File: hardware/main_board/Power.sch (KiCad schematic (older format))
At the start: 12 parts, among them U201 LM1117-5.0

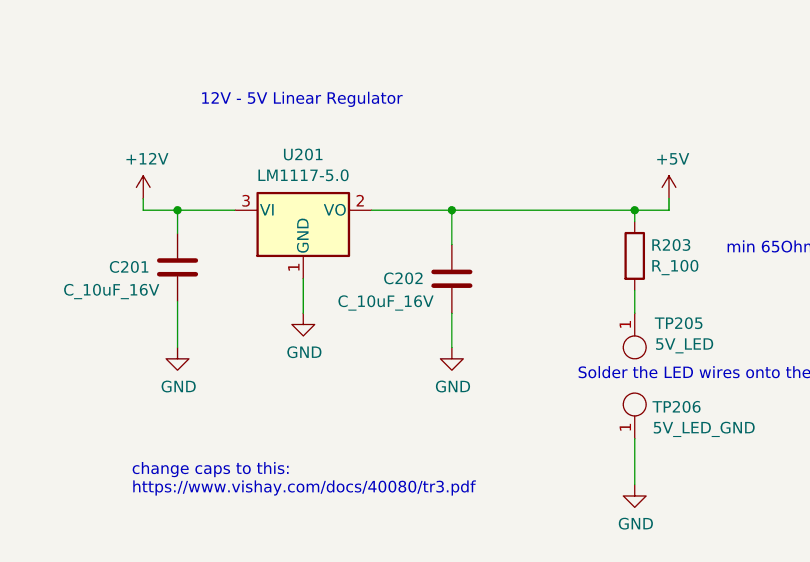
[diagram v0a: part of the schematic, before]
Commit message: added connector for powering limit switches
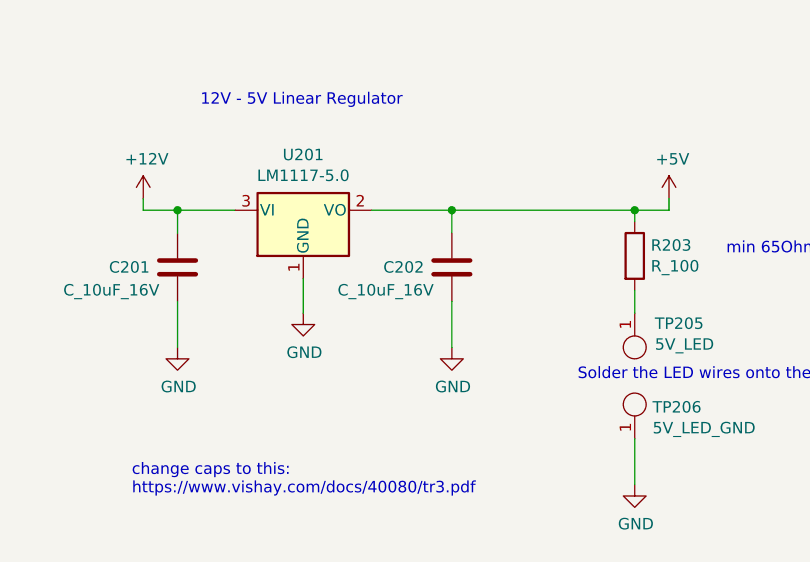
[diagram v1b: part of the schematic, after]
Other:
- moved on the sheet: C202
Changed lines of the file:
@@
 	5250 2400 5600 2400
 Wire Wire Line
-	5600 2400 5600 2550
+	5600 2400 5600 2500
 Connection ~ 5600 2400
 Wire Wire Line
@@
 $EndComp
 Wire Wire Line
-	5600 2850 5600 3000
+	5600 2800 5600 3000
 Text Notes 4500 1950 0    50   ~ 0
 12V - 5V Linear Regulator
@@
 L formula:C_10uF_16V C202
 U 1 1 6239EB03
-P 5600 2700
-F 0 "C202" H 5900 2700 50  0000 R CNN
-F 1 "C_10uF_16V" H 6100 2800 50  0000 R CNN
-F 2 "footprints:C_0805_OEM" H 5638 2550 50  0001 C CNN
-F 3 "http://www.samsungsem.com/kr/support/product-search/mlcc/__icsFiles/afieldfile/2016/01/15/Data%20sheet_CL21A106KOCLRNC.pdf" H 5625 2800 50  0001 C CNN
-F 4 "DK" H 5600 2700 60  0001 C CNN "MFN"
-F 5 "1276-2399-1-ND" H 5600 2700 60  0001 C CNN "MPN"
-F 6 "https://www.digikey.com/product-detail/en/samsung-electro-mechanics/CL21A106KOCLRNC/1276-2399-1-ND/3890485" H 6025 3200 60  0001 C CNN "PurchasingLink"
-	1    5600 2700
-	-1   0    0    1
-$EndComp
+P 5600 2650
+F 0 "C202" H 5900 2650 50  0000 R CNN
+F 1 "C_10uF_16V" H 6100 2750 50  0000 R CNN
+F 2 "footprints:C_0805_OEM" H 5638 2500 50  0001 C CNN
+F 3 "http://www.samsungsem.com/kr/support/product-search/mlcc/__icsFiles/afieldfile/2016/01/15/Data%20sheet_CL21A106KOCLRNC.pdf" H 5625 2750 50  0001 C CNN
+F 4 "DK" H 5600 2650 60  0001 C CNN "MFN"
+F 5 "1276-2399-1-ND" H 5600 2650 60  0001 C CNN "MPN"
+F 6 "https://www.digikey.com/product-detail/en/samsung-electro-mechanics/CL21A106KOCLRNC/1276-2399-1-ND/3890485" H 6025 3150 60  0001 C CNN "PurchasingLink"
+	1    5600 2650
+	-1   0    0    1
+$EndComp

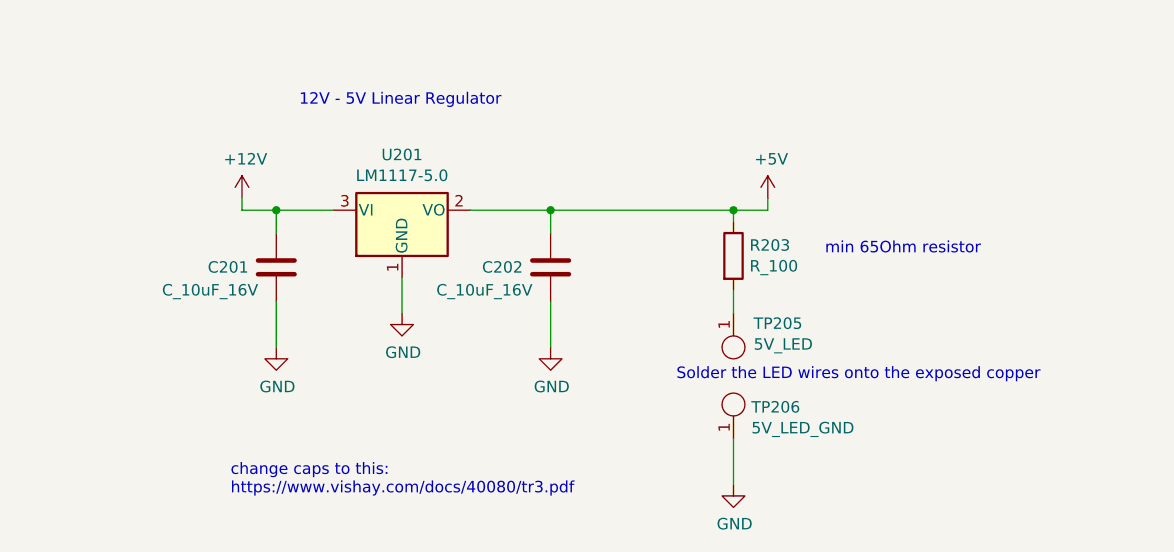
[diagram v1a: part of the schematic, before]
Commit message: Added skittle_pnp symbol and footprint library
Added 10uF tantalum capacitor and diode to the
skittle_pnp symbol and footprints libraries.
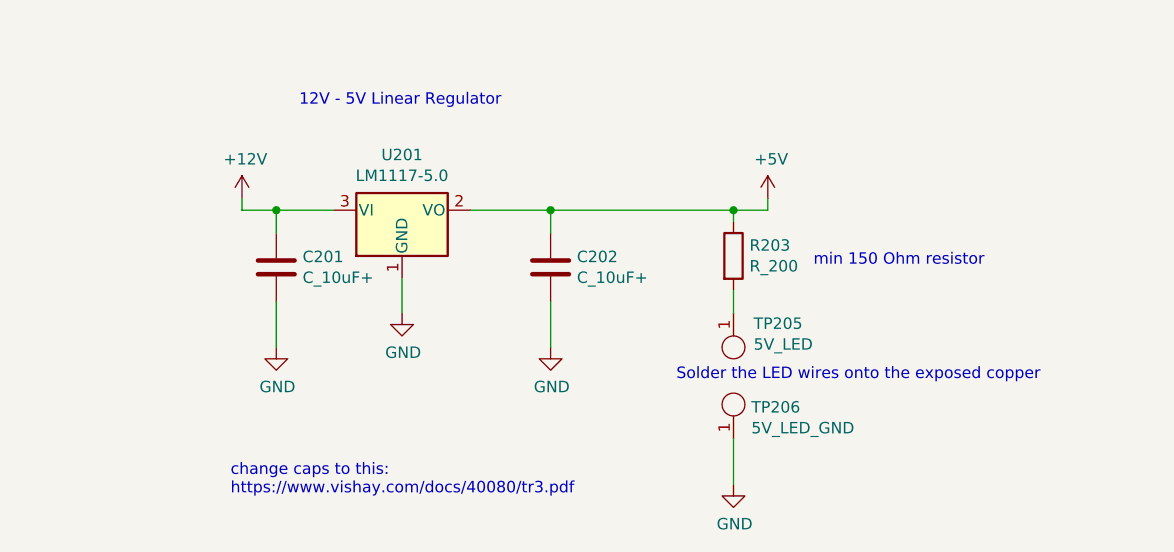
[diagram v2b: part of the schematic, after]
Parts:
- removed C201, C202: C_10uF_16V, footprints:C_0805_OEM, symbol formula:C_10uF_16V
- removed R203: R_100, footprints:R_0805_OEM, symbol formula:R_100
- added C201, C202: C_10uF+, skittle_pnp:T491C105K050AT, symbol skittle_pnp:C_10uF+
- added R203: R_200, footprints:R_0805_OEM, symbol formula:R_200
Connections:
- net +12V: now also C201.1
- net +5V: now also C202.1, R203.1
- net GND: now also C201.2, C202.2
- net at TP205.1: now also R203.2
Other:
- note added: "min 150 Ohm resistor"
- note removed: "min 65Ohm resistor"
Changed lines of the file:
@@
 $Descr A4 11693 8268
 encoding utf-8
-Sheet 2 4
+Sheet 2 5
 Title ""
 Date ""
@@
 	-1   0    0    1
 $EndComp
-$Comp
-L formula:R_100 R203
-U 1 1 61DB93FF
-P 6400 2600
-F 0 "R203" H 6470 2646 50  0000 L CNN
-F 1 "R_100" H 6470 2555 50  0000 L CNN
-F 2 "footprints:R_0805_OEM" H 5600 2750 50  0001 C CNN
-F 3 "https://www.seielect.com/Catalog/SEI-rncp.pdf" H 6100 3100 50  0001 C CNN
-F 4 "DK" H 6400 2600 60  0001 C CNN "MFN"
-F 5 "RNCP0805FTD100RCT-ND" H 5750 2850 60  0001 C CNN "MPN"
-F 6 "https://www.digikey.com/products/en?keywords=RNCP0805FTD100RCT-ND" H 6880 3000 60  0001 C CNN "PurchasingLink"
-	1    6400 2600
-	1    0    0    -1
-$EndComp
 Wire Wire Line
 	6400 2400 6400 2450
@@
 Wire Wire Line
 	6400 2750 6400 2850
-Text Notes 6800 2600 0    50   ~ 0
-min 65Ohm resistor
 $Comp
 L formula:Test_Point_SMD TP206
@@
 	1    0    0    -1
 $EndComp
-$Comp
-L formula:C_10uF_16V C201
-U 1 1 623924BD
-P 4400 2650
-F 0 "C201" H 4700 2650 50  0000 R CNN
-F 1 "C_10uF_16V" H 4900 2750 50  0000 R CNN
-F 2 "footprints:C_0805_OEM" H 4438 2500 50  0001 C CNN
-F 3 "http://www.samsungsem.com/kr/support/product-search/mlcc/__icsFiles/afieldfile/2016/01/15/Data%20sheet_CL21A106KOCLRNC.pdf" H 4425 2750 50  0001 C CNN
-F 4 "DK" H 4400 2650 60  0001 C CNN "MFN"
-F 5 "1276-2399-1-ND" H 4400 2650 60  0001 C CNN "MPN"
-F 6 "https://www.digikey.com/product-detail/en/samsung-electro-mechanics/CL21A106KOCLRNC/1276-2399-1-ND/3890485" H 4825 3150 60  0001 C CNN "PurchasingLink"
-	1    4400 2650
-	-1   0    0    1
-$EndComp
-$Comp
-L formula:C_10uF_16V C202
-U 1 1 6239EB03
-P 5600 2650
-F 0 "C202" H 5900 2650 50  0000 R CNN
-F 1 "C_10uF_16V" H 6100 2750 50  0000 R CNN
-F 2 "footprints:C_0805_OEM" H 5638 2500 50  0001 C CNN
-F 3 "http://www.samsungsem.com/kr/support/product-search/mlcc/__icsFiles/afieldfile/2016/01/15/Data%20sheet_CL21A106KOCLRNC.pdf" H 5625 2750 50  0001 C CNN
-F 4 "DK" H 5600 2650 60  0001 C CNN "MFN"
-F 5 "1276-2399-1-ND" H 5600 2650 60  0001 C CNN "MPN"
-F 6 "https://www.digikey.com/product-detail/en/samsung-electro-mechanics/CL21A106KOCLRNC/1276-2399-1-ND/3890485" H 6025 3150 60  0001 C CNN "PurchasingLink"
-	1    5600 2650
-	-1   0    0    1
-$EndComp
 Text Notes 4200 3650 0    50   ~ 0
 change caps to this:\nhttps://www.vishay.com/docs/40080/tr3.pdf
+$Comp
+L skittle_pnp:C_10uF+ C201
+U 1 1 62AA4E23
+P 4400 2650
+F 0 "C201" H 4515 2696 50  0000 L CNN
+F 1 "C_10uF+" H 4515 2605 50  0000 L CNN
+F 2 "skittle_pnp:T491C105K050AT" H 4438 2500 50  0001 C CNN
+F 3 "https://www.vishay.com/docs/40080/tr3.pdf" H 4400 2650 50  0001 C CNN
+F 4 "https://www.digikey.com/en/products/detail/vishay-sprague/TR3C106K016C0500/13587248" H 4400 2650 50  0001 C CNN "Purchasing Link"
+F 5 "DK" H 4400 2650 50  0001 C CNN "MFN"
+F 6 "718-TR3C106K016C0500CT-ND" H 4400 2650 50  0001 C CNN "MPN"
+	1    4400 2650
+	1    0    0    -1
+$EndComp
+$Comp
+L skittle_pnp:C_10uF+ C202
+U 1 1 62AA54E6
+P 5600 2650
+F 0 "C202" H 5715 2696 50  0000 L CNN
+F 1 "C_10uF+" H 5715 2605 50  0000 L CNN
+F 2 "skittle_pnp:T491C105K050AT" H 5638 2500 50  0001 C CNN
+F 3 "https://www.vishay.com/docs/40080/tr3.pdf" H 5600 2650 50  0001 C CNN
+F 4 "https://www.digikey.com/en/products/detail/vishay-sprague/TR3C106K016C0500/13587248" H 5600 2650 50  0001 C CNN "Purchasing Link"
+F 5 "DK" H 5600 2650 50  0001 C CNN "MFN"
+F 6 "718-TR3C106K016C0500CT-ND" H 5600 2650 50  0001 C CNN "MPN"
+	1    5600 2650
+	1    0    0    -1
+$EndComp
+$Comp
+L formula:R_200 R203
+U 1 1 62AA9E7D
+P 6400 2600
+F 0 "R203" H 6470 2646 50  0000 L CNN
+F 1 "R_200" H 6470 2555 50  0000 L CNN
+F 2 "footprints:R_0805_OEM" H 6330 2600 50  0001 C CNN
+F 3 "https://www.seielect.com/Catalog/SEI-RMCF_RMCP.pdf" H 6480 2600 50  0001 C CNN
+F 4 "DK" H 6400 2600 60  0001 C CNN "MFN"
+F 5 "RMCF0805JT200RCT-ND" H 6400 2600 60  0001 C CNN "MPN"
+F 6 "https://www.digikey.com/products/en?keywords=RMCF0805JT200RCT-ND" H 6880 3000 60  0001 C CNN "PurchasingLink"
+	1    6400 2600
+	1    0    0    -1
+$EndComp
+Text Notes 6750 2650 0    50   ~ 0
+min 150 Ohm resistor
 $EndSCHEMATC

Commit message: final schematic and layout
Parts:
- removed R201: R_100, footprints:R_0805_OEM, symbol formula:R_100
- removed R202: R_500, symbol Device:R
- added C203, C204: C_10uF+, skittle_pnp:T491C105K050AT, symbol skittle_pnp:C_10uF+
- added R201: R_1K, footprints:R_0805_OEM, symbol formula:R_1K
- added R204: R_200, footprints:R_0805_OEM, symbol formula:R_200
- added U202: LM1117-3.3, skittle_pnp:SOT230P700X180-4N, symbol Regulator_Linear:LM1117-3.3
- TP201: value 3.3_LED -> 12V_LED
- TP202: value 3.3_LED_GND -> 12V_LED_GND
- TP203: value 12V_LED -> 3V3_LED
- TP204: value 12V_LED_GND -> 3V3_LED_GND
- U201: footprint (none) -> skittle_pnp:SOT230P700X180-4N
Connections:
- net +12V: now also C203.1, R201.1, U202.3 (VI)
- net +3V3: now also C204.1, R204.1, U202.2 (VO)
- net GND: now also C203.2, C204.2, U202.1 (GND)
- net at TP203.1: now also R204.2
- net at TP201.1: now also R201.2
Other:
- note added: "12V - 3V Linear Regulator"
- note added: "12V Indicator LED"
- note added: "5V Indicator LED"
- note added: "Solder on the LED on the exposed copper"
- note removed: "Solder the LED wires onto the exposed copper"
- note removed: "min 150 Ohm resistor"
- note removed: "min 65 Ohms"
- note removed: "solder the LED wires to the exposed copper"
